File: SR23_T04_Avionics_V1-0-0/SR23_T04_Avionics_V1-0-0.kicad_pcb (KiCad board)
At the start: 2 copper layers, 46 parts, among them J1 QWIIC, J11 Conn_01x02, J12 Conn_01x02, J13 Conn_01x02, J14 BAT_CHARGE, J2 QWIIC, J3 QWIIC, J4 BAT_POWER, J5 BAT_uC, J6 BAT_PCB+, J7 Conn_01x03, J8 Conn_01x03, J9 Conn_01x03, Q2 BSP75N, Q3 BSP75N, Q4 BSP75N, SW1 SW_DIP_x02, U1 MCP73831-2-OT, U2 MS563702BA03-50, U3 MPU-6050, U4 MOUDLE-SEEEDUINO-XIAO-ESP32C3

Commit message: wip: PCB rooting
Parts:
- added H1: MountingHole, MountingHole:MountingHole_3.2mm_M3_ISO7380, F.Cu at (101.6, 91.4)
- added H2: MountingHole, MountingHole:MountingHole_3.2mm_M3_ISO7380, F.Cu at (101.6, 106.7)
- added H3: MountingHole, MountingHole:MountingHole_3.2mm_M3_ISO7380, F.Cu at (185.4, 106.7)
- added H4: MountingHole, MountingHole:MountingHole_3.2mm_M3_ISO7380, F.Cu at (185.4, 91.4)
- moved J4 26.2 mm to (185.4, 97.8), turned to -90 degrees
- moved R5 8.89 mm to (142.2, 104.1)
- moved R6 8.89 mm to (142.2, 101.6)
- moved R7 8.89 mm to (142.2, 94.0)
- moved R8 8.89 mm to (142.2, 91.4)
- moved R3 8.89 mm to (141.0, 91.4)
- moved R4 8.89 mm to (141.0, 94.0)
- moved SW1 8.02 mm to (179.1, 90.2), turned to -90 degrees
- moved J14 5.08 mm to (160.0, 91.4), turned to -90 degrees
- moved C3 2.84 mm to (166.4, 105.4)
- moved J8 2.84 mm to (163.8, 101.6)
- moved J9 2.84 mm to (163.8, 105.4)
- moved J7 2.83 mm to (163.8, 97.8)
- moved J5 1.80 mm to (170.2, 92.7), turned to 180 degrees
- moved C5 1.41 mm to (171.7, 107.0)
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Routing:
- net DIP_1b: track 0.00 -> 114.4 mm
- net +3.3V: track 0.00 -> 63.5 mm, vias 0 -> 4
- net SCL: track 0.00 -> 61.3 mm
- net DIP_2b: track 0.00 -> 56.6 mm
- net SDA: track 0.00 -> 48.1 mm
- net VUSB: track 0.00 -> 31.6 mm
- net GND: track 0.00 -> 21.5 mm, vias 0 -> 7
- net DIP_1a: track 0.00 -> 10.3 mm
- net DIP_2a: track 0.00 -> 7.40 mm
- net Servo1: track 0.00 -> 6.37 mm
- net Servo3: track 0.00 -> 5.86 mm
- net Servo2: track 0.00 -> 5.84 mm
- net Net-(D3-Pad1): track 0.00 -> 1.61 mm
- net Net-(D2-Pad1): track 0.00 -> 1.27 mm
- added copper zone on B.Cu, net GND

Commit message: wip: working on avionics
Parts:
- moved R6 1.05 mm to (142.5, 102.6), turned to 0 degrees
- moved R12 0.78 mm to (117.3, 104.6)
- moved R14 0.78 mm to (126.2, 104.6)
- moved R13 0.70 mm to (108.5, 104.6)
- moved R5 0.57 mm to (142.5, 104.6), turned to 0 degrees
- moved D7 0.30 mm to (124.2, 104.6)
- moved D6 0.23 mm to (106.5, 104.6)
- moved D5 0.23 mm to (115.4, 104.6)
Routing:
- net DIP_1b: track 114.4 -> 181.2 mm
- net OUT2: track 0.00 -> 35.8 mm, vias 0 -> 1
- net OUT4: track 0.00 -> 34.5 mm
- net SDA: track 48.1 -> 77.5 mm, vias 0 -> 1
- net OUT3: track 0.00 -> 25.8 mm
- net GND: track 21.5 -> 27.9 mm, vias 7 -> 10
- net Net-(J11-Pad2): track 0.00 -> 6.05 mm
- net Net-(J12-Pad2): track 0.00 -> 5.98 mm
- net Net-(J13-Pad2): track 0.00 -> 5.95 mm
- net DIP_2b: track 56.6 -> 61.2 mm
- net SCL: track 61.3 -> 64.9 mm, vias 0 -> 1
- net MON_BAT_uC: track 0.00 -> 1.73 mm
- net MON_BAT_POWER: track 0.00 -> 1.73 mm
- net Net-(D7-Pad1): track 0.00 -> 1.22 mm
- net Net-(D6-Pad1): track 0.00 -> 1.22 mm
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
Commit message: wip: rooting of the board completed - waiting on review
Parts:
- moved R3 1.55 mm to (139.4, 91.7)
- moved R4 1.55 mm to (139.4, 94.2)
- moved R8 1.05 mm to (141.2, 91.7)
- moved R7 1.05 mm to (141.2, 94.2)
- moved C5 0.72 mm to (172.2, 106.4)
- moved C6 0.51 mm to (180.3, 106.2)
- moved R14 0.25 mm to (126.5, 104.6)
- moved D7 0.25 mm to (124.5, 104.6)
- turned U2 to -90 degrees
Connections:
- Q2 pad 1: OUT3 -> OUT2
- Q3 pad 1: OUT2 -> OUT1
- Q4 pad 1: OUT4 -> OUT3
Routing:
- net +3.3V: track 63.5 -> 121.1 mm
- net GND: track 27.9 -> 63.7 mm, vias 10 -> 19
- net OUT4: track 34.5 -> 0.00 mm
- net OUT1: track 0.00 -> 33.4 mm, vias 0 -> 1
- net SDA: track 77.5 -> 98.4 mm, vias 1 -> 4
- net SCL: track 64.9 -> 84.6 mm, vias 1 -> 0
- net OUT3: track 25.8 -> 10.0 mm
- net OUT2: track 35.8 -> 22.7 mm
- net STAT: track 0.00 -> 6.69 mm
- net DIP_1b: track 181.2 -> 175.5 mm, vias 0 -> 1
- net MON_BAT_uC: track 1.73 -> 6.05 mm, vias 0 -> 1
- net Net-(R1-Pad1): track 0.00 -> 3.42 mm
- net MON_BAT_POWER: track 1.73 -> 4.49 mm
- net Net-(C5-Pad1): track 0.00 -> 2.40 mm
- net Net-(C6-Pad1): track 0.00 -> 1.92 mm
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
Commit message: feat: Version 1.0.0 of the AV-Flow PCB
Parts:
- added D4: GREEN, LED_SMD:LED_0201_0603Metric_Pad0.64x0.40mm_HandSolder, F.Cu at (161.8, 108.0)
- added R11: 540, Resistor_SMD:R_0201_0603Metric_Pad0.64x0.40mm_HandSolder, F.Cu at (159.0, 108.0)
- moved J4 0.78 mm to (186.2, 97.8)
- renumbered D6 to D5, D5 to D6, J3 to J1, J12 to J11, J11 to J12, J1 to J3, Q3 to Q1, Q4 to Q3, R13 to R12, R12 to R13
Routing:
- net GND: track 63.7 -> 78.8 mm, vias 19 -> 20
- net OUT3: track 10.0 -> 20.5 mm
- net OUT4: track 0.00 -> 5.69 mm, vias 0 -> 1
- net +3.3V: track 121.1 -> 126.1 mm
- net Net-(D4-Pad2): track 0.00 -> 2.00 mm
- net SDA: track 98.4 -> 99.5 mm
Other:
- board outline added: 91.4 x 22.9 mm
- board text added: "+"
- board text added: "CHARGE"
- board text added: "GND"
- board text added: "OUT1"
- board text added: "OUT2"
- board text added: "OUT3"
- board text added: "Project: AV-Flow Version: 1.0.0 Date: 11.04.2023 Author: Florian Patiny Co-author: Luc Patiny"
- board text added: "Servo1"
- board text added: "Servo2"
- board text added: "Servo3"

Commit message: wip: PCB V2
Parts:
- removed J13: Conn_01x02, Connector_JST:JST_PH_B2B-PH-K_1x02_P2.00mm_Vertical
- added J10: Screw_Terminal_01x02, TerminalBlock_MetzConnect:TerminalBlock_MetzConnect_Type086_RT03402HBLC_1x02_P3.81mm_Horizontal, F.Cu at (117.0, 106.0)
- C1, C2, C3, C4, C5, C6: footprint Capacitor_SMD:C_0201_0603Metric_Pad0.64x0.40mm_HandSolder -> Capacitor_SMD:C_0805_2012Metric_Pad1.18x1.45mm_HandSolder; moved to B.Cu
- D1: footprint LED_SMD:LED_0201_0603Metric_Pad0.64x0.40mm_HandSolder -> LED_SMD:LED_0805_2012Metric_Pad1.15x1.40mm_HandSolder; moved to B.Cu
- D2, D3, D5, D6, D7: footprint LED_SMD:LED_0201_0603Metric_Pad0.64x0.40mm_HandSolder -> LED_SMD:LED_0805_2012Metric_Pad1.15x1.40mm_HandSolder
- D4: value GREEN -> LED; footprint LED_SMD:LED_0201_0603Metric_Pad0.64x0.40mm_HandSolder -> LED_SMD:LED_0805_2012Metric_Pad1.15x1.40mm_HandSolder
- J11, J12: value Conn_01x02 -> Screw_Terminal_01x02; footprint Connector_JST:JST_PH_B2B-PH-K_1x02_P2.00mm_Vertical -> TerminalBlock_MetzConnect:TerminalBlock_MetzConnect_Type086_RT03402HBLC_1x02_P3.81mm_Horizontal
- Q1, Q2, Q3, U1, U2, U3: moved to B.Cu
- R1, R10, R2, R3, R4, R5, R6, R7, R8, R9: footprint Resistor_SMD:R_0201_0603Metric_Pad0.64x0.40mm_HandSolder -> Resistor_SMD:R_0805_2012Metric_Pad1.20x1.40mm_HandSolder; moved to B.Cu
- R11, R12, R13, R14: footprint Resistor_SMD:R_0201_0603Metric_Pad0.64x0.40mm_HandSolder -> Resistor_SMD:R_0805_2012Metric_Pad1.20x1.40mm_HandSolder
- moved C6 67.7 mm to (114.3, 91.2)
- moved C5 66.0 mm to (108.0, 91.2)
- moved C2 65.9 mm to (111.3, 91.2), turned to -90 degrees
- moved U3 59.2 mm to (119.4, 91.2), turned to 180 degrees
- moved U2 43.6 mm to (128.5, 91.2)
- moved C3 34.0 mm to (135.6, 90.9)
- moved C4 31.8 mm to (138.9, 106.7), turned to -90 degrees
- moved D4 29.2 mm to (132.8, 104.1), turned to -90 degrees
- moved R11 26.1 mm to (132.8, 107.9), turned to 90 degrees
- moved R2 25.8 mm to (142.5, 106.7)
- moved R1 25.1 mm to (145.8, 106.7)
- moved C1 23.0 mm to (149.4, 106.7)
- moved U1 22.4 mm to (147.8, 99.8), turned to 0 degrees
- moved H3 19.4 mm to (179.6, 88.1)
- moved J4 18.8 mm to (169.9, 107.2), turned to 180 degrees
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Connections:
- J12 pad 2: Net-(J12-Pad2) -> Net-(Q3-Pad2)
- Q2 pad 2: Net-(J12-Pad2) -> Net-(Q2-Pad2)
- Q3 pad 1: OUT3 -> OUT4
- Q3 pad 2: Net-(J13-Pad2) -> Net-(Q3-Pad2)
- R11 pad 1: OUT4 -> OUT3
- R13 pad 2: Net-(J12-Pad2) -> Net-(Q2-Pad2)
- R14 pad 2: Net-(J13-Pad2) -> Net-(Q3-Pad2)
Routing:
- net DIP_1b: track 175.5 -> 0.00 mm, vias 1 -> 0
- net +3.3V: track 126.1 -> 0.00 mm, vias 4 -> 0
- net SDA: track 99.5 -> 0.00 mm, vias 4 -> 0
- net SCL: track 84.6 -> 0.00 mm
- net GND: track 78.8 -> 0.00 mm, vias 20 -> 0
- net DIP_2b: track 62.2 -> 0.00 mm
- net OUT1: track 33.4 -> 0.00 mm, vias 1 -> 0
- net VUSB: track 31.6 -> 0.00 mm
- net OUT2: track 22.7 -> 0.00 mm, vias 1 -> 0
- net OUT3: track 20.5 -> 0.00 mm
- net DIP_1a: track 10.6 -> 0.00 mm
- net DIP_2a: track 7.40 -> 0.00 mm
- net STAT: track 6.69 -> 0.00 mm
- net Servo1: track 6.37 -> 0.00 mm
- net MON_BAT_uC: track 6.05 -> 0.00 mm, vias 1 -> 0
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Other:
- board outline removed

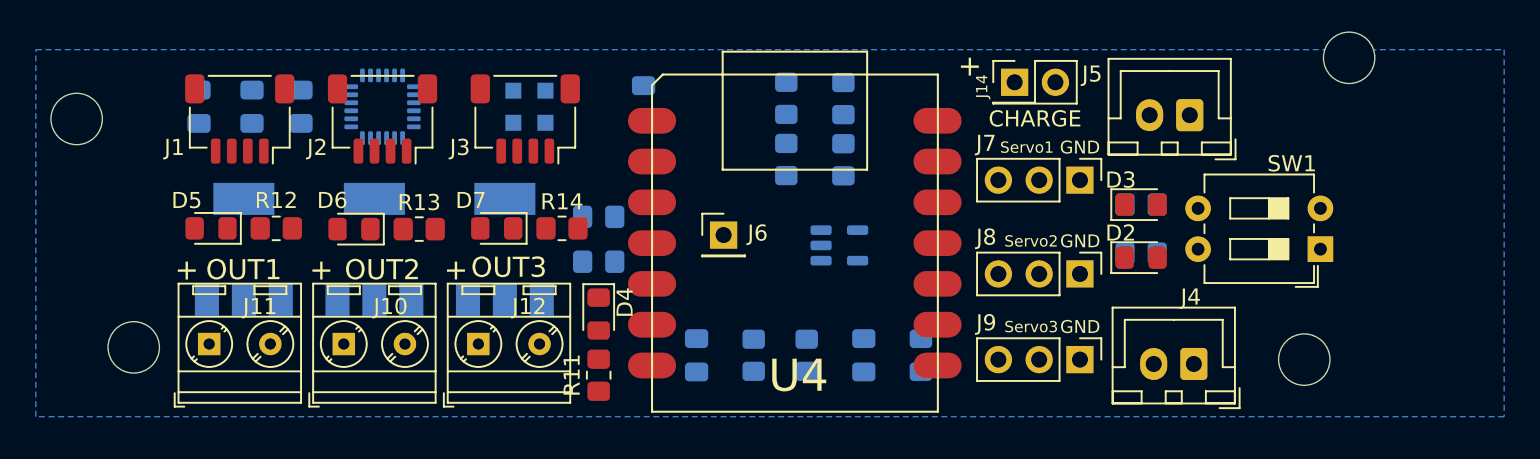
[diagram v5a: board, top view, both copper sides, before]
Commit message: feat: new board V2 dual sided
closes: https://github.com/Hackuarium/Avionics/issues/7
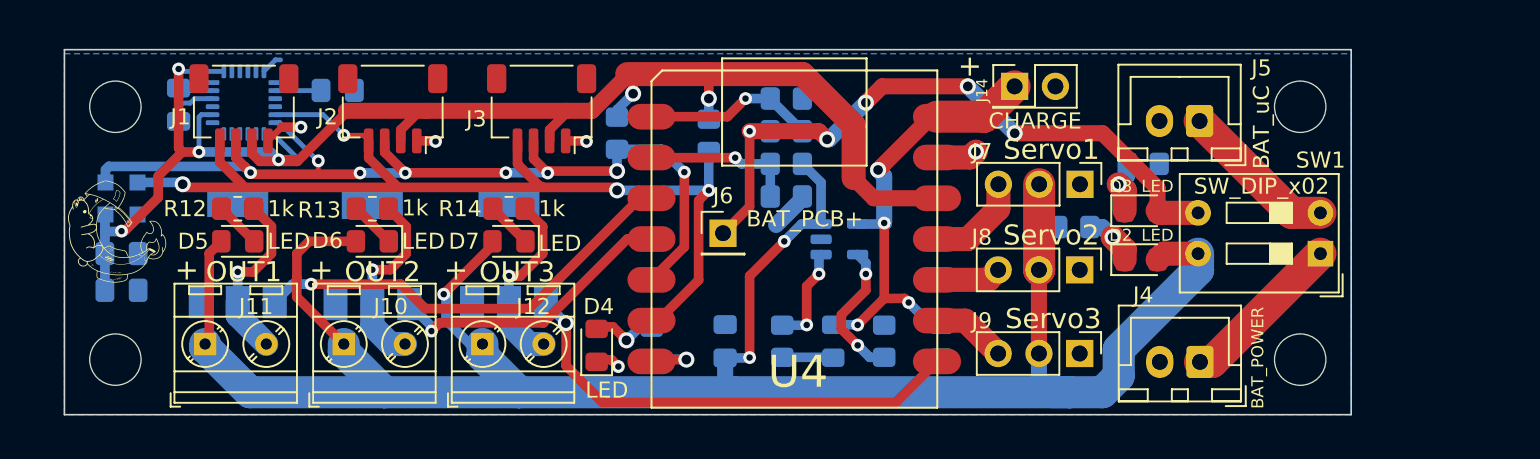
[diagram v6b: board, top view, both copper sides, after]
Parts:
- R11: moved to B.Cu
- SW1: footprint Button_Switch_THT:SW_DIP_SPSTx02_Slide_6.7x6.64mm_W7.62mm_P2.54mm_LowProfile -> Button_Switch_THT:SW_DIP_SPSTx02_Slide_9.78x7.26mm_W7.62mm_P2.54mm
- U2: value MS563702BA03-50 -> MS563702
- moved C3 34.6 mm to (103.1, 102.6), turned to 0 degrees
- moved U2 26.0 mm to (103.1, 96.9), turned to 0 degrees
- moved Q1 16.6 mm to (110.4, 100.2)
- moved Q3 16.5 mm to (127.3, 100.2)
- moved C2 12.2 mm to (103.1, 100.3), turned to 0 degrees
- moved R5 10.4 mm to (139.7, 93.0), turned to 90 degrees
- moved C5 8.70 mm to (116.6, 90.2), turned to 0 degrees
- moved U3 8.64 mm to (110.7, 90.9), turned to 90 degrees
- moved C6 7.62 mm to (106.7, 91.1)
- moved R4 6.11 mm to (144.5, 96.8), turned to 0 degrees
- moved D1 5.53 mm to (147.4, 105.8)
- moved R6 5.33 mm to (134.0, 92.8), turned to 90 degrees
- moved R1 4.90 mm to (150.6, 105.8)
- moved C1 4.90 mm to (154.2, 105.8), turned to -90 degrees
- moved R9 4.50 mm to (162.4, 98.7), turned to 180 degrees
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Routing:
- net DIP_1b: track 0.00 -> 139.2 mm, vias 0 -> 3
- net +3.3V: track 0.00 -> 93.3 mm, vias 0 -> 6
- net SCL: track 0.00 -> 64.5 mm, vias 0 -> 4
- net SDA: track 0.00 -> 58.6 mm, vias 0 -> 8
- net DIP_2b: track 0.00 -> 41.9 mm, vias 0 -> 5
- net OUT4: track 0.00 -> 29.6 mm, vias 0 -> 1
- net VUSB: track 0.00 -> 28.6 mm, vias 0 -> 4
- net OUT1: track 0.00 -> 27.4 mm, vias 0 -> 1
- net OUT2: track 0.00 -> 18.3 mm, vias 0 -> 1
- net GND: track 0.00 -> 17.8 mm, vias 0 -> 5
- net Net-(J10-Pad2): track 0.00 -> 11.8 mm, vias 0 -> 1
- net Net-(J12-Pad2): track 0.00 -> 11.6 mm, vias 0 -> 1
- net Net-(J11-Pad2): track 0.00 -> 11.0 mm, vias 0 -> 1
- net MON_BAT_uC: track 0.00 -> 10.7 mm, vias 0 -> 1
- net DIP_1a: track 0.00 -> 10.3 mm
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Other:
- board outline added: 80.1 x 22.7 mm
- board text added: "AV-Flow V2.0.0 30.07.2023"
- board text removed: "GND"
- board text removed: "Project: AV-Flow Version: 1.0.0 Date: 11.04.2023 Author: Florian Patiny Co-author: Luc Patiny"
